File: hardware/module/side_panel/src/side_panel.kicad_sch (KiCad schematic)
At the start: 34 parts, among them J1 Top Connector, J2 Bottom Connecor, J3 Conn_01x05, J4 Conn_01x09, M1 GA12-N20 12V 60rpm, Q1 AP2302B, U1 QRE1113GR, U10 NUP4202, U2 QRE1113GR, U3 QRE1113GR, U4 QRE1113GR, U5 QRE1113GR, U6 QRE1113GR, U7 PY32F003F1xPx, U8 L9110S, U9 74LVC1G66

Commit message: changed hole patern encoder wheel
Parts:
- added H1, H10, H2, H3, H4, H5, H6, H7, H8, H9: MountingHole, MountingHole:MountingHole_2.7mm, symbol Mechanical:MountingHole

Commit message: Increase encoder LED current to 70mA and make make two pairs of 3 to reduce power draw
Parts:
- removed R2, R3, R5, R7: 100R, Resistor_SMD:R_0805_2012Metric, symbol Device:R
- R7: renamed from R9; value 100R -> 20R
- R8: renamed from R11; value 100R -> 20R
- renumbered R15 to R10, R13 to R11, R4 to R2, R6 to R3, R8 to R4, R10 to R5, R12 to R6, R14 to R9
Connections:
- net +5V: no longer U3.1 (A), U4.1 (A), U5.1 (A), U6.1 (A)
- net at Q1.3 (D), R7.1: now also R8.2; no longer R8.1
- net at U4.2 (K): now also U6.1 (A)
- net at U1.2 (K): now also U3.1 (A)
- net at U6.2 (K): now also R8.1; no longer R8.2
- net at U3.2 (K): now also U5.1 (A)
- net at U2.2 (K): now also U4.1 (A)
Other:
- note added: "Vs = 5V Vf = 1.2V If = 70mA R = [ Vs - ( 3 x Vf ) ] / If = 20 Ohm"
- moved on the sheet: Q1, R1, R10, R2, R3, R4, R5, R6, R7, R8, R9, U1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

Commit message: Change from absolute encoder to incremental encoder.
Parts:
- removed R4, R5, R6: 20K, Resistor_SMD:R_0805_2012Metric, symbol Device:R
- removed R8: 20R, Resistor_SMD:R_0805_2012Metric, symbol Device:R
- removed U4, U5, U6: QRE1113GR, OptoDevice:OnSemi_CASE100CY, symbol Sensor_Proximity:QRE1113GR
- U1, U2, U3: value QRE1113GR -> ITR8307
- renumbered R7 to R4, R9 to R5, R10 to R6, R11 to R7, U7 to U4, U8 to U5, U9 to U6, U10 to U7
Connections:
- net IR Sens Ch 4 is gone; now on net IR Sens Z: U4.3 (PA4)
- net IR Sens Ch 6 is gone; now on net IR Sens B: U4.2 (PA3)
- net +5V: no longer U2.1 (A)
- net Column End: now also U4.20 (PA1); no longer U4.8 (PA12)
- net Debug Pin 1: now also U4.17 (PF1-OSC_OUT); no longer U4.16 (PF0-OSC_IN)
- net Debug Pin 2: now also U4.16 (PF0-OSC_IN); no longer U4.17 (PF1-OSC_OUT)
- net Motor IN_A: now also U4.5 (PA6); no longer U4.12 (PB5)
- net Motor IN_B: now also U4.6 (PA7); no longer U4.5 (PA6)
- net at R4.1: now also U2.2 (K); no longer Q1.3 (D)
- net at R4.2: now also Q1.3 (D)
- net at U3.2 (K): now also U2.1 (A)
- net IR Sens Ch 1 renamed IR Sens A
- net IR Sens A: now also U4.4 (PA5); no longer U4.19 (PA0)
- net IR Sens Ch 2 renamed IR Sens B
- net IR Sens B: no longer U4.4 (PA5)
- net IR Sens Ch 3 renamed IR Sens Z
- net IR Sens Z: no longer U4.20 (PA1)
- net IR Sens Ch 5 renamed IR Sens LED
- net IR Sens LED: now also J4.9 (Pin_9), R5.1, R6.1
- removed net IR Sense LED: J4.9 (Pin_9), R5.1, R6.1, U4.6 (PA7)
- no-connect marks 3 -> 6
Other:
- note added: "IR Optical Encoder"
- note removed: "6 Ch IR Optical Encoder"
- moved on the sheet: Q1, R1, R2, R3, R4, R5, R6, U1, U2, U3

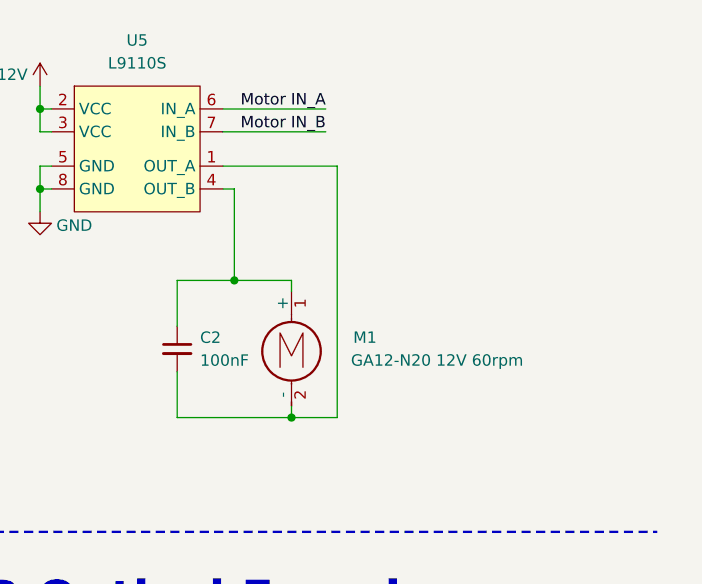
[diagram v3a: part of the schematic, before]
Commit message: Side panel 5.0.1 swap motor polarity
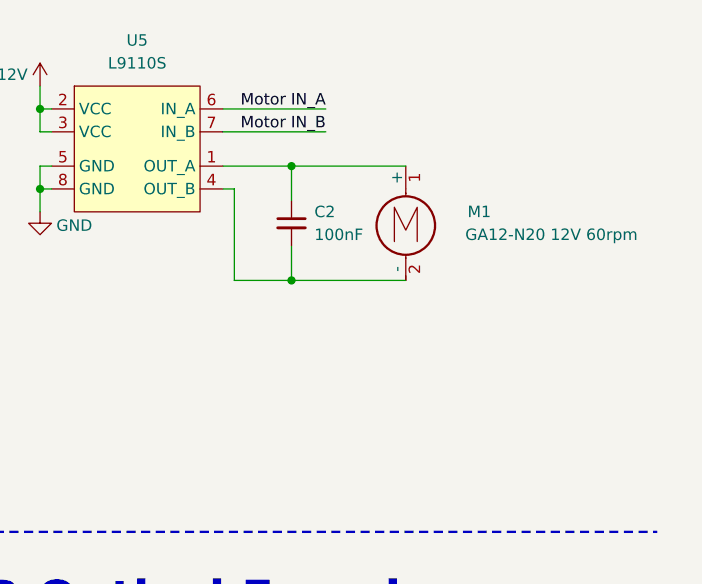
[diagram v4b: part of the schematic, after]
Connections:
- net at C2.2, M1.2 (-): now also U5.4 (OUT_B); no longer U5.1 (OUT_A)
- net at C2.1, M1.1 (+): now also U5.1 (OUT_A); no longer U5.4 (OUT_B)
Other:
- moved on the sheet: C2, M1
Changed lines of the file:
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@@
 		(title "Side Panel")
 		(date "${DATE}")
-		(rev "5.0.0")
+		(rev "5.0.1")
 		(company "OpenFlap")
 		(comment 1 "${GIT_TAG}")
@@
 	)
 	(junction
+		(at 156.21 48.26)
+		(diameter 0)
+		(color 0 0 0 0)
+	)
+	(junction
 		(at 41.91 119.38)
 		(diameter 0)
@@
 	)
 	(junction
-		(at 58.42 121.92)
+		(at 156.21 60.96)
 		(diameter 0)
 		(color 0 0 0 0)
 	)
 	(junction
-		(at 156.21 76.2)
+		(at 58.42 121.92)
 		(diameter 0)
 		(color 0 0 0 0)
@@
 	)
 	(junction
-		(at 149.86 60.96)
-		(diameter 0)
-		(color 0 0 0 0)
-	)
-	(junction
 		(at 41.91 121.92)
 		(diameter 0)
@@
 	(wire
 		(pts
-			(xy 156.21 62.23) (xy 156.21 60.96)
+			(xy 17.78 204.47) (xy 19.05 204.47)
 		)
 		(stroke
@@
 	(wire
 		(pts
-			(xy 17.78 204.47) (xy 19.05 204.47)
+			(xy 156.21 48.26) (xy 168.91 48.26)
 		)
 		(stroke
@@
 	(wire
 		(pts
+			(xy 156.21 60.96) (xy 168.91 60.96)
+		)
+		(stroke
+			(width 0)
+			(type default)
+		)
+	)
+	(wire
+		(pts
 			(xy 39.37 129.54) (xy 41.91 129.54)
 		)
@@
 	(wire
 		(pts
-			(xy 161.29 76.2) (xy 156.21 76.2)
+			(xy 125.73 185.42) (xy 125.73 179.07)
 		)
 		(stroke
@@
 	(wire
 		(pts
-			(xy 125.73 185.42) (xy 125.73 179.07)
+			(xy 34.29 39.37) (xy 49.53 39.37)
 		)
 		(stroke
@@
 	(wire
 		(pts
-			(xy 34.29 39.37) (xy 49.53 39.37)
+			(xy 34.29 54.61) (xy 49.53 54.61)
 		)
 		(stroke
@@
 	(wire
 		(pts
-			(xy 34.29 54.61) (xy 49.53 54.61)
+			(xy 106.68 179.07) (xy 125.73 179.07)
 		)
 		(stroke
@@
 	(wire
 		(pts
-			(xy 106.68 179.07) (xy 125.73 179.07)
+			(xy 156.21 57.15) (xy 156.21 60.96)
 		)
 		(stroke
@@
 	(wire
 		(pts
-			(xy 161.29 48.26) (xy 161.29 76.2)
-		)
-		(stroke
-			(width 0)
-			(type default)
-		)
-	)
-	(wire
-		(pts
 			(xy 74.93 130.81) (xy 74.93 140.97)
 		)
@@
 	(wire
 		(pts
-			(xy 143.51 60.96) (xy 149.86 60.96)
-		)
-		(stroke
-			(width 0)
-			(type default)
-		)
-	)
-	(wire
-		(pts
 			(xy 36.83 78.74) (xy 49.53 78.74)
 		)
@@
 	(wire
 		(pts
-			(xy 156.21 76.2) (xy 156.21 74.93)
-		)
-		(stroke
-			(width 0)
-			(type default)
-		)
-	)
-	(wire
-		(pts
 			(xy 58.42 148.59) (xy 58.42 151.13)
 		)
@@
 	(wire
 		(pts
-			(xy 73.66 201.93) (xy 73.66 204.47)
+			(xy 156.21 48.26) (xy 156.21 52.07)
 		)
 		(stroke
@@
 	(wire
 		(pts
-			(xy 55.88 111.76) (xy 74.93 111.76)
+			(xy 73.66 201.93) (xy 73.66 204.47)
 		)
 		(stroke
@@
 	(wire
 		(pts
-			(xy 31.75 111.76) (xy 43.18 111.76)
+			(xy 55.88 111.76) (xy 74.93 111.76)
 		)
 		(stroke
@@
 	(wire
 		(pts
-			(xy 58.42 127) (xy 58.42 129.54)
+			(xy 31.75 111.76) (xy 43.18 111.76)
 		)
 		(stroke
@@
 	(wire
 		(pts
-			(xy 156.21 60.96) (xy 149.86 60.96)
+			(xy 58.42 127) (xy 58.42 129.54)
 		)
 		(stroke
@@
 	(wire
 		(pts
-			(xy 148.59 48.26) (xy 161.29 48.26)
+			(xy 148.59 48.26) (xy 156.21 48.26)
 		)
 		(stroke
@@
 	(wire
 		(pts
-			(xy 143.51 71.12) (xy 143.51 76.2)
-		)
-		(stroke
-			(width 0)
-			(type default)
-		)
-	)
-	(wire
-		(pts
 			(xy 19.05 248.92) (xy 38.1 248.92)
 		)
@@
 	(wire
 		(pts
-			(xy 19.05 246.38) (xy 38.1 246.38)
+			(xy 149.86 60.96) (xy 156.21 60.96)
 		)
 		(stroke
@@
 	(wire
 		(pts
-			(xy 77.47 130.81) (xy 77.47 132.08)
+			(xy 19.05 246.38) (xy 38.1 246.38)
 		)
 		(stroke
@@
 	(wire
 		(pts
-			(xy 74.93 111.76) (xy 74.93 120.65)
+			(xy 77.47 130.81) (xy 77.47 132.08)
 		)
 		(stroke
@@
 	(wire
 		(pts
-			(xy 143.51 76.2) (xy 156.21 76.2)
+			(xy 74.93 111.76) (xy 74.93 120.65)
 		)
 		(stroke
@@
 	(wire
 		(pts
-			(xy 143.51 66.04) (xy 143.51 60.96)
-		)
-		(stroke
-			(width 0)
-			(type default)
-		)
-	)
-	(wire
-		(pts
 			(xy 58.42 124.46) (xy 58.42 127)
 		)
@@
 	(symbol
 		(lib_id "Motor:Motor_DC")
-		(at 156.21 67.31 0)
+		(at 168.91 53.34 0)
 		(unit 1)
 		(exclude_from_sim no)
@@
 		(dnp no)
 		(property "Reference" "M1"
-			(at 163.068 67.31 0)
+			(at 175.768 53.34 0)
 			(effects
 				(font
@@
 		)
 		(property "Value" "GA12-N20 12V 60rpm"
-			(at 162.814 69.85 0)
+			(at 175.514 55.88 0)
 			(effects
 				(font
@@
 		)
 		(property "Footprint" "GA12-N20:GA12-N20 Motor Vertical"
-			(at 156.21 69.596 0)
+			(at 168.91 55.626 0)
 			(effects
 				(font
@@
 		)
 		(property "Datasheet" "~"
-			(at 156.21 69.596 0)
+			(at 168.91 55.626 0)
 			(effects
 				(font
@@
 		)
 		(property "Description" "DC Motor"
-			(at 156.21 67.31 0)
+			(at 168.91 53.34 0)
 			(effects
 				(font
@@
 	(symbol
 		(lib_id "Device:C_Small")
-		(at 143.51 68.58 0)
+		(at 156.21 54.61 0)
 		(unit 1)
 		(exclude_from_sim no)
@@
 		(dnp no)
 		(property "Reference" "C2"
-			(at 146.05 67.3163 0)
+			(at 158.75 53.3463 0)
 			(effects
 				(font
@@
 		)
 		(property "Value" "100nF"
-			(at 146.05 69.8563 0)
+			(at 158.75 55.8863 0)
 			(effects
 				(font
@@
 		)
 		(property "Footprint" "Capacitor_SMD:C_0805_2012Metric"
-			(at 143.51 68.58 0)
+			(at 156.21 54.61 0)
 			(effects
 				(font
@@
 		)
 		(property "Datasheet" "~"
-			(at 143.51 68.58 0)
+			(at 156.21 54.61 0)
 			(effects
 				(font
@@
 		)
 		(property "Description" "Unpolarized capacitor, small symbol"
-			(at 143.51 68.58 0)
+			(at 156.21 54.61 0)
 			(effects
 				(font

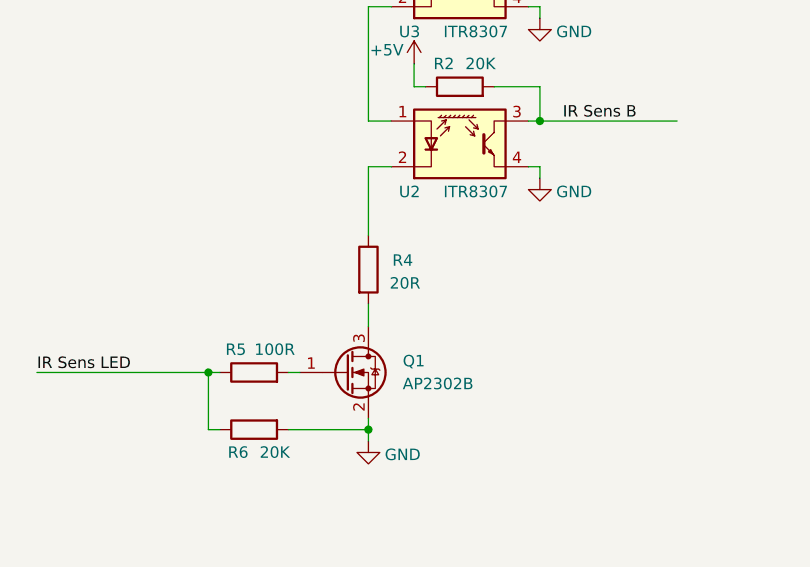
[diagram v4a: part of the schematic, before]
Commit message: Change sidepanel IR resistor to 15ohm and finalize encoder wheel design
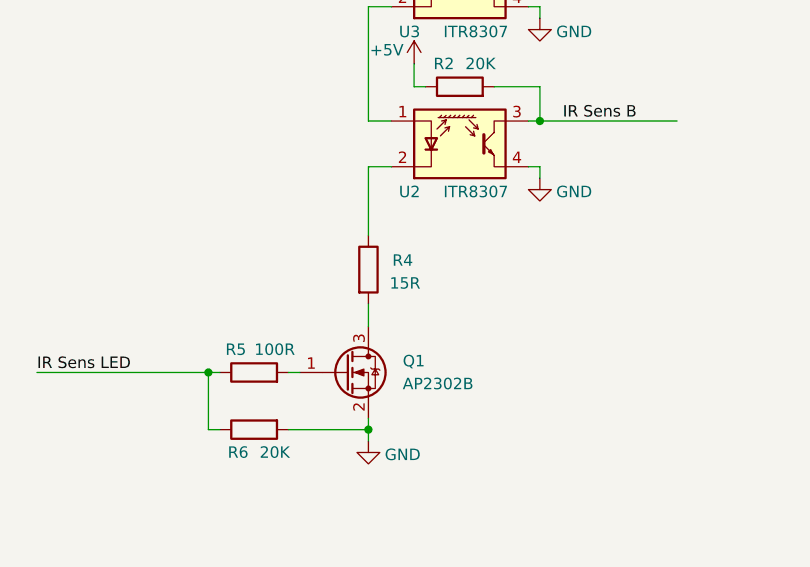
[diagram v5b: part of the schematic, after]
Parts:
- R4: value 20R -> 15R
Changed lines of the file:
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@@
 		(title "Side Panel")
 		(date "${DATE}")
-		(rev "5.0.1")
+		(rev "5.0.2")
 		(company "OpenFlap")
 		(comment 1 "${GIT_TAG}")
@@
 			)
 		)
-		(property "Value" "20R"
+		(property "Value" "15R"
 			(at 147.574 169.164 0)
 			(effects

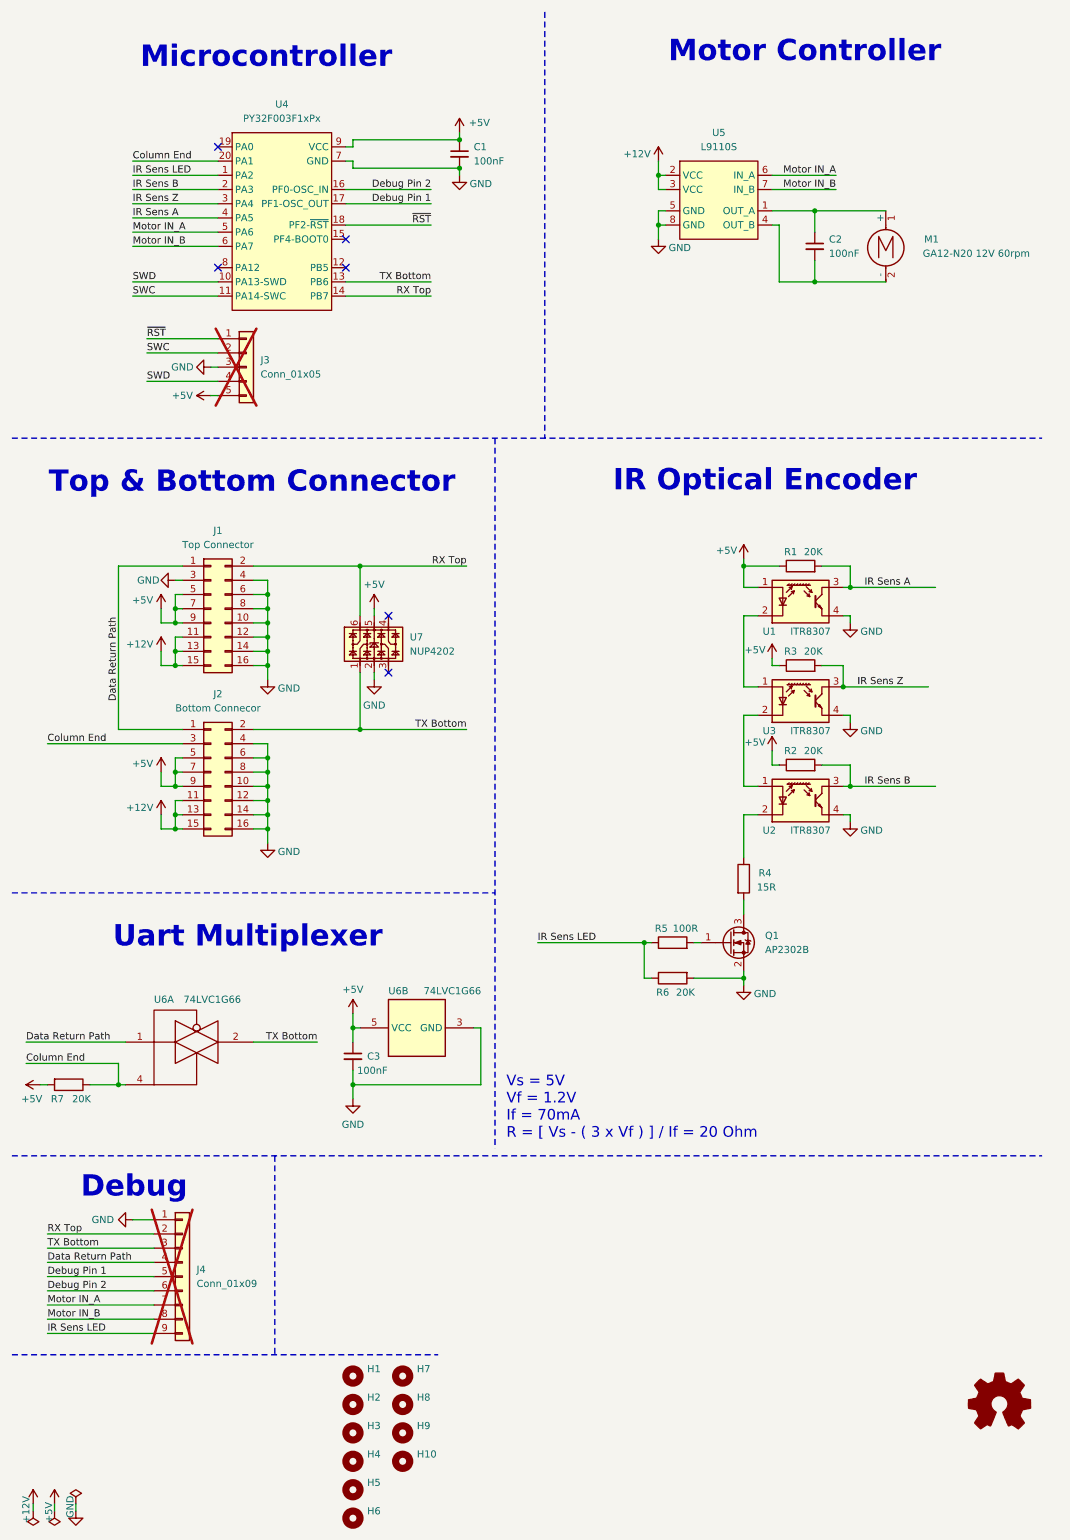
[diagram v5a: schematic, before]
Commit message: Rework top connector and side panel connections to increase power rating. Switch from 2 channel to 4 channel incremental encoder.
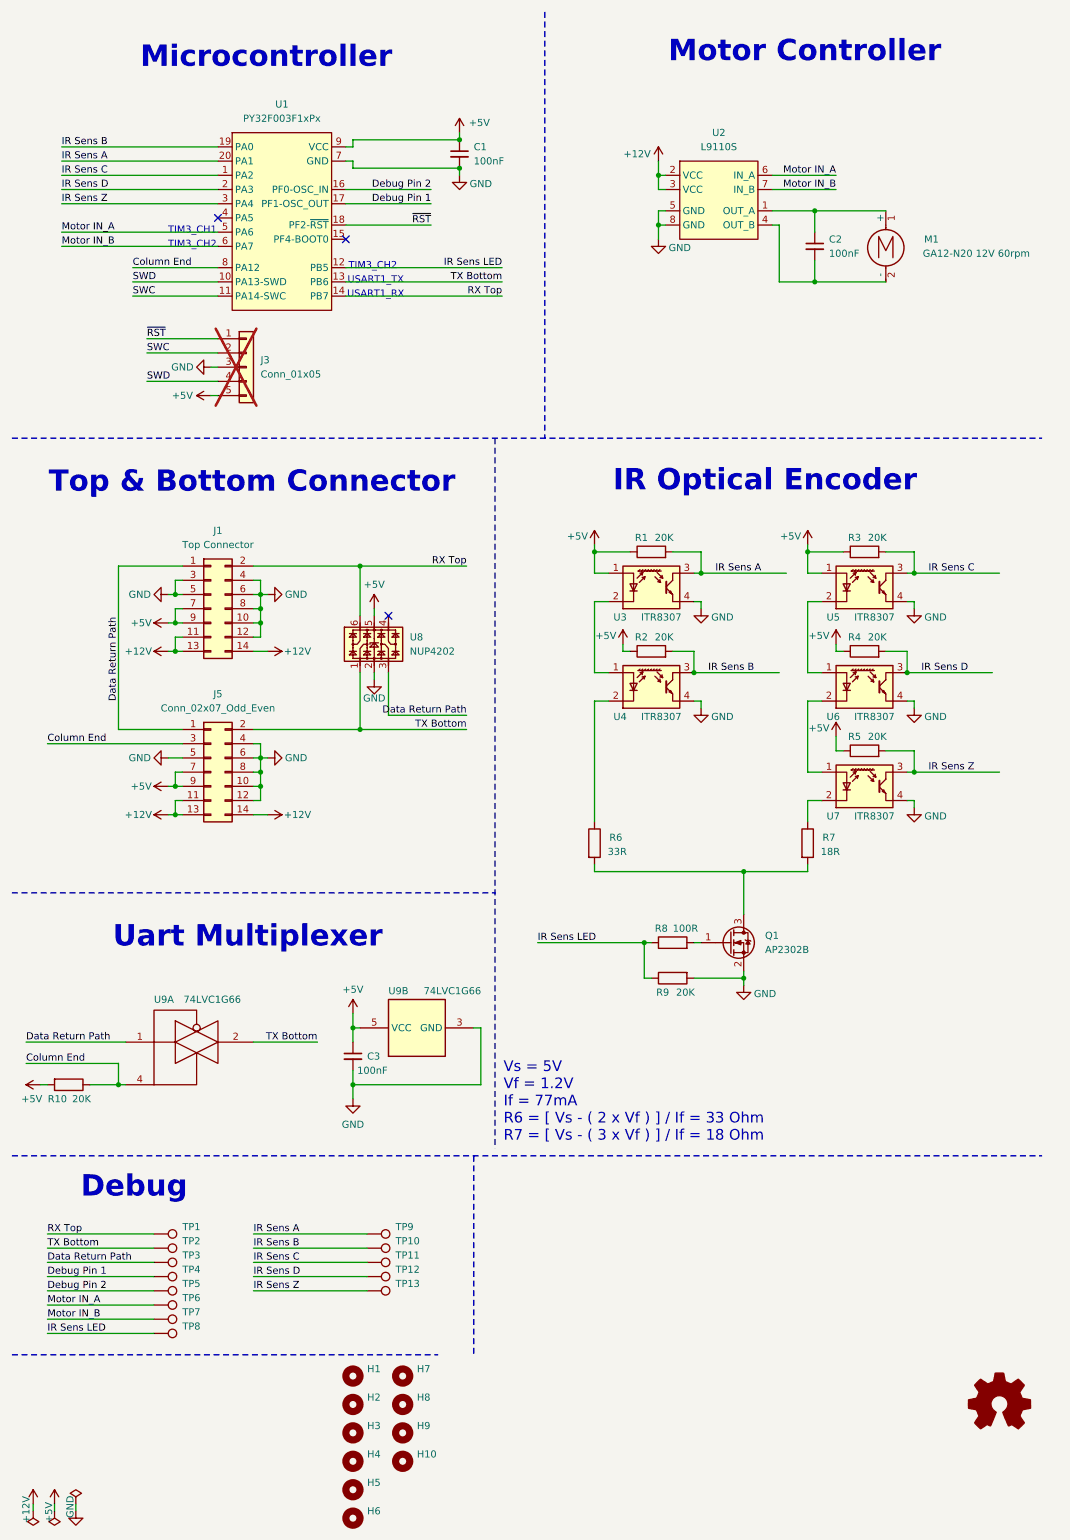
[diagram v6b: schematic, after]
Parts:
- removed J1: Top Connector, Connector_PinHeader_2.54mm:PinHeader_2x08_P2.54mm_Horizontal, symbol Connector_Generic:Conn_02x08_Odd_Even
- removed J2: Bottom Connecor, Connector_PinSocket_2.54mm:PinSocket_2x08_P2.54mm_Horizontal, symbol Connector_Generic:Conn_02x08_Odd_Even
- removed J4: Conn_01x09, Connector_PinHeader_2.54mm:PinHeader_1x09_P2.54mm_Vertical, symbol Connector_Generic:Conn_01x09
- added J1: Top Connector, Connector_PinHeader_2.54mm:PinHeader_2x07_P2.54mm_Horizontal, symbol Connector_Generic:Conn_02x07_Odd_Even
- added J5: Conn_02x07_Odd_Even, Connector_PinSocket_2.54mm:PinSocket_2x07_P2.54mm_Horizontal, symbol Connector_Generic:Conn_02x07_Odd_Even
- added R1, R2: 20K, Resistor_SMD:R_0805_2012Metric, symbol Device:R
- added R6: 33R, Resistor_SMD:R_0805_2012Metric, symbol Device:R
- added TP1, TP10, TP11, TP12, TP13, TP2, TP3, TP4, TP5, TP6, TP7, TP8, TP9: TestPoint, TestPoint:TestPoint_THTPad_D2.5mm_Drill1.2mm, symbol Connector:TestPoint
- added U3, U4: ITR8307, OptoDevice:OnSemi_CASE100CY, symbol Sensor_Proximity:QRE1113GR
- R7: renamed from R4; value 15R -> 18R
- renumbered R7 to R10, R1 to R3, R3 to R4, R2 to R5, R5 to R8, R6 to R9, U4 to U1, U5 to U2, U1 to U5, U3 to U6, U2 to U7, U7 to U8, U6 to U9
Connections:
- net +12V: now also J1.11 (Pin_11), J1.13 (Pin_13), J1.14 (Pin_14), J5.11 (Pin_11), J5.13 (Pin_13), J5.14 (Pin_14)
- net +5V: now also J1.7 (Pin_7), J1.9 (Pin_9), J5.7 (Pin_7), J5.9 (Pin_9), R1.1, R2.1, U3.1 (A)
- net Column End: now also U1.8 (PA12), J5.3 (Pin_3); no longer U1.20 (PA1)
- net Data Return Path: now also U8.3, J1.1 (Pin_1), J5.1 (Pin_1), TP3.1
- net Debug Pin 1: now also TP4.1
- net Debug Pin 2: now also TP5.1
- net GND: now also J1.10 (Pin_10), J1.12 (Pin_12), J1.3 (Pin_3), J1.4 (Pin_4), J1.5 (Pin_5), J1.6 (Pin_6), J1.8 (Pin_8), J5.10 (Pin_10), J5.12 (Pin_12), J5.4 (Pin_4), J5.5 (Pin_5), J5.6 (Pin_6), J5.8 (Pin_8), U3.4, U4.4
- net IR Sens A: now also U1.20 (PA1), R1.2, TP9.1, U3.3; no longer R3.2, U1.4 (PA5), U5.3
- net IR Sens B: now also U1.19 (PA0), R2.2, TP10.1, U4.3; no longer R5.2, U1.2 (PA3), U7.3
- net IR Sens LED: now also U1.12 (PB5), TP8.1; no longer U1.1 (PA2)
- net IR Sens Z: now also R5.2, U7.3, TP13.1; no longer R4.2, U6.3
- net Motor IN_A: now also TP6.1
- net Motor IN_B: now also TP7.1
- net RX Top: now also J1.2 (Pin_2), TP1.1
- net TX Bottom: now also J5.2 (Pin_2), TP2.1
- net at Q1.3 (D), R7.2: now also R6.2
- new net: U3.2 (K), U4.1 (A)
- new net: R6.1, U4.2 (K)
- new net IR Sens C: R3.2, TP11.1, U1.1 (PA2), U5.3
- new net IR Sens D: R4.2, TP12.1, U1.2 (PA3), U6.3
- no-connect marks 6 -> 3
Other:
- note added: "TIM3_CH1"
- note added: "TIM3_CH2"
- note added: "USART1_RX"
- note added: "USART1_TX"
- note added: "Vs = 5V Vf = 1.2V If = 77mA R6 = [ Vs - ( 2 x Vf ) ] / If = 33 Ohm R7 = [ Vs - ( 3 x Vf ) ] / If = 18 Ohm"
- note removed: "Vs = 5V Vf = 1.2V If = 70mA R = [ Vs - ( 3 x Vf ) ] / If = 20 Ohm"
- moved on the sheet: R3, R4, R5, R7, U5, U6, U7
